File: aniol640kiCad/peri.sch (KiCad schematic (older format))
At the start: 6 parts

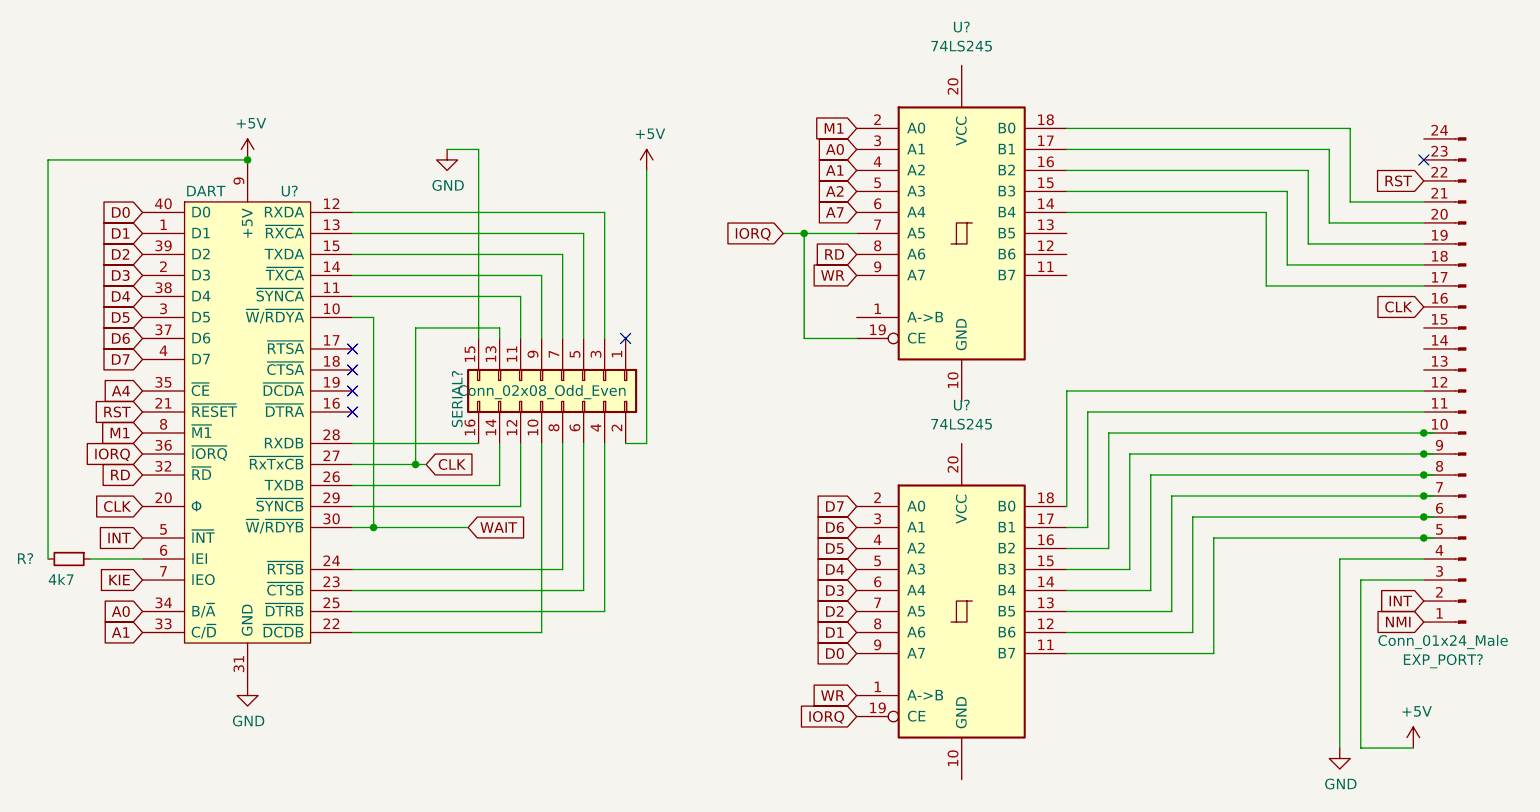
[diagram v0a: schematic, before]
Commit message: Added basic PS2 keyboard support
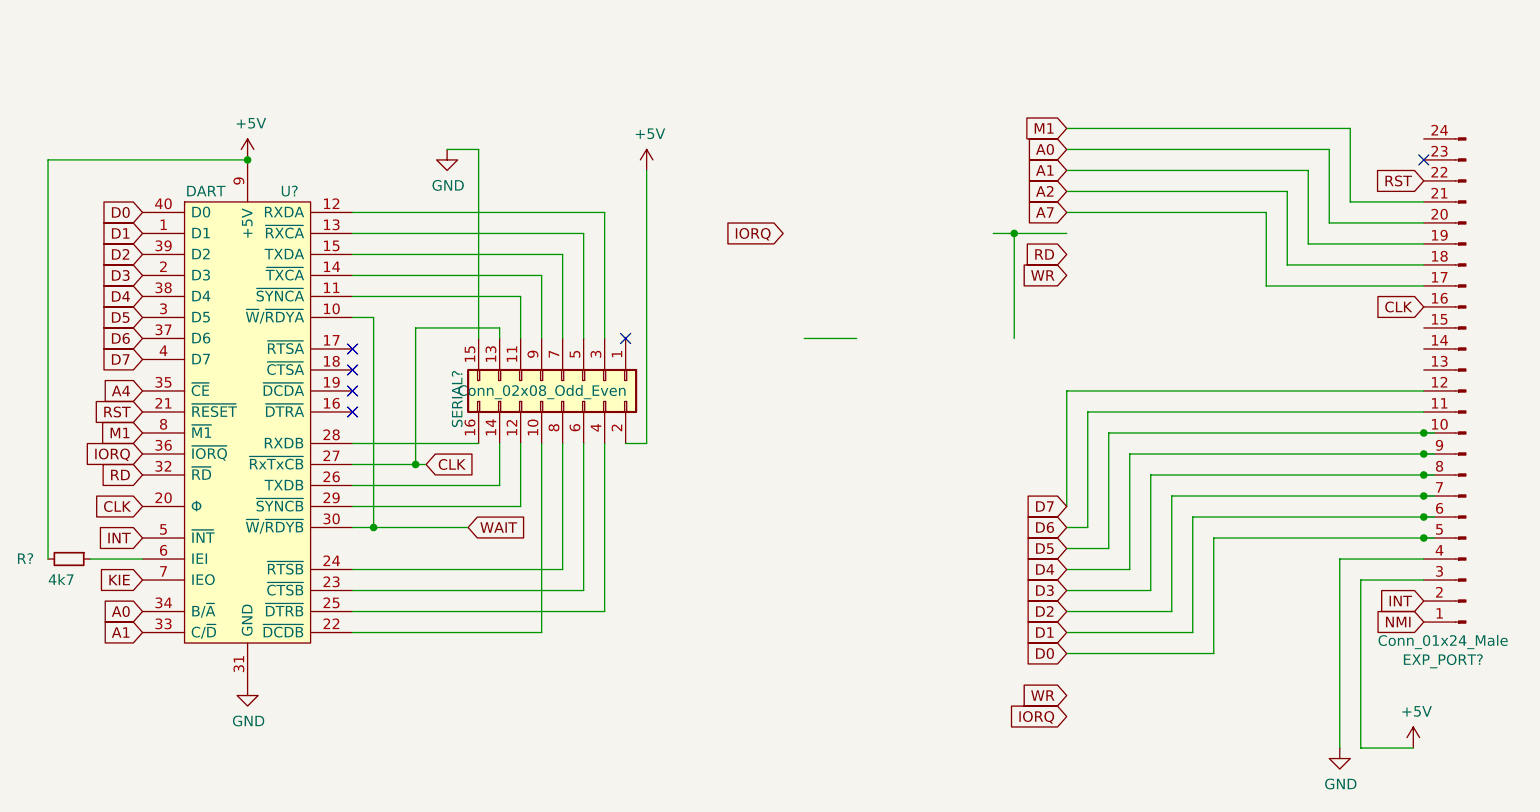
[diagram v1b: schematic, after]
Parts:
- removed U? (x2): 74LS245, symbol 74xx:74LS245
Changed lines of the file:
@@
 Text GLabel 8400 3250 0    50   Input ~ 0
 INT
-Text GLabel 5700 3500 0    50   Input ~ 0
+Text GLabel 6700 3500 0    50   Input ~ 0
 D0
-Text GLabel 5700 3400 0    50   Input ~ 0
+Text GLabel 6700 3400 0    50   Input ~ 0
 D1
-Text GLabel 5700 3300 0    50   Input ~ 0
+Text GLabel 6700 3300 0    50   Input ~ 0
 D2
-Text GLabel 5700 3200 0    50   Input ~ 0
+Text GLabel 6700 3200 0    50   Input ~ 0
 D3
-Text GLabel 5700 3100 0    50   Input ~ 0
+Text GLabel 6700 3100 0    50   Input ~ 0
 D4
-Text GLabel 5700 3000 0    50   Input ~ 0
+Text GLabel 6700 3000 0    50   Input ~ 0
 D5
-Text GLabel 5700 2900 0    50   Input ~ 0
+Text GLabel 6700 2900 0    50   Input ~ 0
 D6
-Text GLabel 5700 2800 0    50   Input ~ 0
+Text GLabel 6700 2800 0    50   Input ~ 0
 D7
-Text GLabel 5700 1700 0    50   Input ~ 0
+Text GLabel 6700 1700 0    50   Input ~ 0
 WR
-Text GLabel 5700 1600 0    50   Input ~ 0
+Text GLabel 6700 1600 0    50   Input ~ 0
 RD
 Text GLabel 5350 1500 0    50   Input ~ 0
@@
 Text GLabel 8400 1850 0    50   Input ~ 0
 CLK
-Text GLabel 5700 1400 0    50   Input ~ 0
+Text GLabel 6700 1400 0    50   Input ~ 0
 A7
-Text GLabel 5700 1300 0    50   Input ~ 0
+Text GLabel 6700 1300 0    50   Input ~ 0
 A2
-Text GLabel 5700 1200 0    50   Input ~ 0
+Text GLabel 6700 1200 0    50   Input ~ 0
 A1
-Text GLabel 5700 1100 0    50   Input ~ 0
+Text GLabel 6700 1100 0    50   Input ~ 0
 A0
-Text GLabel 5700 1000 0    50   Input ~ 0
+Text GLabel 6700 1000 0    50   Input ~ 0
 M1
 Text GLabel 8400 1250 0    50   Input ~ 0
@@
 Wire Wire Line
 	2050 3050 2300 3050
-$Comp
-L 74xx:74LS245 U?
-U 1 1 622D7911
-P 6200 3300
-F 0 "U?" H 6200 4281 50  0000 C CNN
-F 1 "74LS245" H 6200 4190 50  0000 C CNN
-F 2 "" H 6200 3300 50  0001 C CNN
-F 3 "http://www.ti.com/lit/gpn/sn74LS245" H 6200 3300 50  0001 C CNN
-	1    6200 3300
-	1    0    0    -1
-$EndComp
 Wire Wire Line
 	8000 3050 8400 3050
@@
 Wire Wire Line
 	8450 2950 8400 2950
-Text GLabel 5700 3700 0    50   Input ~ 0
+Text GLabel 6700 3700 0    50   Input ~ 0
 WR
-Text GLabel 5700 3800 0    50   Input ~ 0
+Text GLabel 6700 3800 0    50   Input ~ 0
 IORQ
-$Comp
-L 74xx:74LS245 U?
-U 1 1 6230E5FB
-P 6200 1500
-F 0 "U?" H 6200 2481 50  0000 C CNN
-F 1 "74LS245" H 6200 2390 50  0000 C CNN
-F 2 "" H 6200 1500 50  0001 C CNN
-F 3 "http://www.ti.com/lit/gpn/sn74LS245" H 6200 1500 50  0001 C CNN
-	1    6200 1500
-	1    0    0    -1
-$EndComp
-Wire Wire Line
-	5700 1500 5450 1500
-Wire Wire Line
-	5450 1500 5450 2000
+Wire Wire Line
+	6700 1500 6450 1500
+Wire Wire Line
+	6450 1500 6450 2000
 Wire Wire Line
 	5450 2000 5700 2000
-Connection ~ 5450 1500
-Wire Wire Line
-	5450 1500 5350 1500
+Connection ~ 6450 1500
+Wire Wire Line
+	6450 1500 6350 1500
 Wire Wire Line
 	6700 1000 8050 1000

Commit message: Updated the schematic
- added inverted DART clock
- added power-up reset
- changed to the more simplified ROM address decoding
- removed battery backup for RAM
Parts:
- added R?: R_Small, symbol Device:R_Small
- added U?: 74LS14, symbol 74xx:74LS14
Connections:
- wire segments 92 -> 53
- no-connect marks 6 -> 5
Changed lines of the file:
@@
 Text GLabel 8400 3250 0    50   Input ~ 0
 INT
-Text GLabel 6700 3500 0    50   Input ~ 0
-D0
-Text GLabel 6700 3400 0    50   Input ~ 0
-D1
-Text GLabel 6700 3300 0    50   Input ~ 0
-D2
-Text GLabel 6700 3200 0    50   Input ~ 0
-D3
-Text GLabel 6700 3100 0    50   Input ~ 0
-D4
-Text GLabel 6700 3000 0    50   Input ~ 0
-D5
-Text GLabel 6700 2900 0    50   Input ~ 0
-D6
-Text GLabel 6700 2800 0    50   Input ~ 0
-D7
-Text GLabel 6700 1700 0    50   Input ~ 0
+Text GLabel 8400 2050 0    50   Input ~ 0
 WR
-Text GLabel 6700 1600 0    50   Input ~ 0
+Text GLabel 8400 1950 0    50   Input ~ 0
 RD
-Text GLabel 5350 1500 0    50   Input ~ 0
+Text GLabel 8400 2150 0    50   Input ~ 0
 IORQ
 Text GLabel 8400 1850 0    50   Input ~ 0
 CLK
-Text GLabel 6700 1400 0    50   Input ~ 0
+Text GLabel 8400 1750 0    50   Input ~ 0
 A7
-Text GLabel 6700 1300 0    50   Input ~ 0
+Text GLabel 8400 1650 0    50   Input ~ 0
 A2
-Text GLabel 6700 1200 0    50   Input ~ 0
+Text GLabel 8400 1550 0    50   Input ~ 0
 A1
-Text GLabel 6700 1100 0    50   Input ~ 0
+Text GLabel 8400 1450 0    50   Input ~ 0
 A0
-Text GLabel 6700 1000 0    50   Input ~ 0
+Text GLabel 8400 1350 0    50   Input ~ 0
 M1
 Text GLabel 8400 1250 0    50   Input ~ 0
@@
 L power:+5V #PWR?
 U 1 1 62294225
-P 4700 1200
+P 5650 1200
 AR Path="/62294225" Ref="#PWR?"  Part="1"
 AR Path="/6228D96B/62294225" Ref="#PWR?"  Part="1"
-F 0 "#PWR?" H 4700 1050 50  0001 C CNN
-F 1 "+5V" H 4715 1373 50  0000 C CNN
-F 2 "" H 4700 1200 50  0001 C CNN
-F 3 "" H 4700 1200 50  0001 C CNN
-	1    4700 1200
+F 0 "#PWR?" H 5650 1050 50  0001 C CNN
+F 1 "+5V" H 5665 1373 50  0000 C CNN
+F 2 "" H 5650 1200 50  0001 C CNN
+F 3 "" H 5650 1200 50  0001 C CNN
+	1    5650 1200
 	1    0    0    -1
 $EndComp
@@
 Wire Wire Line
 	3300 2600 3600 2600
-NoConn ~ 4600 2000
 Wire Wire Line
 	3300 2700 4000 2700
@@
 	3900 1100 3900 2000
 Wire Wire Line
-	4600 2500 4700 2500
-Wire Wire Line
-	4700 2500 4700 1200
+	5650 2500 5650 1200
 Wire Wire Line
 	2050 3050 2300 3050
@@
 Wire Wire Line
 	8450 2950 8400 2950
-Text GLabel 6700 3700 0    50   Input ~ 0
-WR
-Text GLabel 6700 3800 0    50   Input ~ 0
-IORQ
-Wire Wire Line
-	6700 1500 6450 1500
-Wire Wire Line
-	6450 1500 6450 2000
-Wire Wire Line
-	5450 2000 5700 2000
-Connection ~ 6450 1500
-Wire Wire Line
-	6450 1500 6350 1500
-Wire Wire Line
-	6700 1000 8050 1000
-Wire Wire Line
-	8050 1000 8050 1350
-Wire Wire Line
-	8050 1350 8400 1350
-Wire Wire Line
-	6700 1100 7950 1100
-Wire Wire Line
-	7950 1100 7950 1450
-Wire Wire Line
-	7950 1450 8400 1450
-Wire Wire Line
-	6700 1200 7850 1200
-Wire Wire Line
-	7850 1200 7850 1550
-Wire Wire Line
-	7850 1550 8400 1550
-Wire Wire Line
-	6700 1300 7750 1300
-Wire Wire Line
-	7750 1300 7750 1650
-Wire Wire Line
-	7750 1650 8400 1650
-Wire Wire Line
-	6700 1400 7650 1400
-Wire Wire Line
-	7650 1400 7650 1750
-Wire Wire Line
-	7650 1750 8400 1750
-Connection ~ 8400 2450
-Connection ~ 8400 2550
-Connection ~ 8400 2650
-Connection ~ 8400 2750
-Connection ~ 8400 2850
-Connection ~ 8400 2950
-Wire Wire Line
-	6700 2800 6700 2250
-Wire Wire Line
-	6700 2250 8400 2250
-Wire Wire Line
-	6700 2900 6800 2900
-Wire Wire Line
-	6800 2900 6800 2350
-Wire Wire Line
-	6800 2350 8400 2350
-Wire Wire Line
-	6700 3000 6900 3000
-Wire Wire Line
-	6900 3000 6900 2450
-Wire Wire Line
-	6900 2450 8400 2450
-Wire Wire Line
-	6700 3100 7000 3100
-Wire Wire Line
-	7000 3100 7000 2550
-Wire Wire Line
-	7000 2550 8400 2550
-Wire Wire Line
-	6700 3200 7100 3200
-Wire Wire Line
-	7100 3200 7100 2650
-Wire Wire Line
-	7100 2650 8400 2650
-Wire Wire Line
-	6700 3300 7200 3300
-Wire Wire Line
-	7200 3300 7200 2750
-Wire Wire Line
-	7200 2750 8400 2750
-Wire Wire Line
-	6700 3400 7300 3400
-Wire Wire Line
-	7300 3400 7300 2850
-Wire Wire Line
-	7300 2850 8400 2850
-Wire Wire Line
-	6700 3500 7400 3500
-Wire Wire Line
-	7400 3500 7400 2950
-Wire Wire Line
-	7400 2950 8400 2950
+$Comp
+L 74xx:74LS14 U?
+U 6 1 6320FDDD
+P 4900 2000
+F 0 "U?" H 4900 2317 50  0000 C CNN
+F 1 "74LS14" H 4900 2226 50  0000 C CNN
+F 2 "" H 4900 2000 50  0001 C CNN
+F 3 "http://www.ti.com/lit/gpn/sn74LS14" H 4900 2000 50  0001 C CNN
+	6    4900 2000
+	1    0    0    -1
+$EndComp
+$Comp
+L Device:R_Small R?
+U 1 1 6321FB1E
+P 5200 1750
+F 0 "R?" H 5259 1796 50  0000 L CNN
+F 1 "R_Small" H 5259 1705 50  0000 L CNN
+F 2 "" H 5200 1750 50  0001 C CNN
+F 3 "~" H 5200 1750 50  0001 C CNN
+	1    5200 1750
+	1    0    0    -1
+$EndComp
+Wire Wire Line
+	5200 1650 5200 1500
+Wire Wire Line
+	5200 2000 5200 1850
+Wire Wire Line
+	5200 1500 4400 1500
+Connection ~ 4400 1500
+Wire Wire Line
+	4600 2500 5650 2500
+Text GLabel 8400 2250 0    50   Input ~ 0
+D7
+Text GLabel 8400 2350 0    50   Input ~ 0
+D6
+Text GLabel 8400 2450 0    50   Input ~ 0
+D5
+Text GLabel 8400 2550 0    50   Input ~ 0
+D4
+Text GLabel 8400 2650 0    50   Input ~ 0
+D3
+Text GLabel 8400 2750 0    50   Input ~ 0
+D2
+Text GLabel 8400 2850 0    50   Input ~ 0
+D1
+Text GLabel 8400 2950 0    50   Input ~ 0
+D0
 $EndSCHEMATC
